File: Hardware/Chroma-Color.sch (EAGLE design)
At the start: 92 parts, among them J1 15-91-1102, J2 87832-6422, J3 1775470-6, J4 D2514-6V0C-AR-WD, J7 26-64-4040, U1 EP4CE6E22C8N, U2 ADP3338AKCZ-3.3-RL, U3 ADP3338AKCZ-2.5-RL, U4 NCV565ST12T3G, U5 M25P40-VMN6TPBCT, X1 ASDMB-50.000MHZ-LC-T

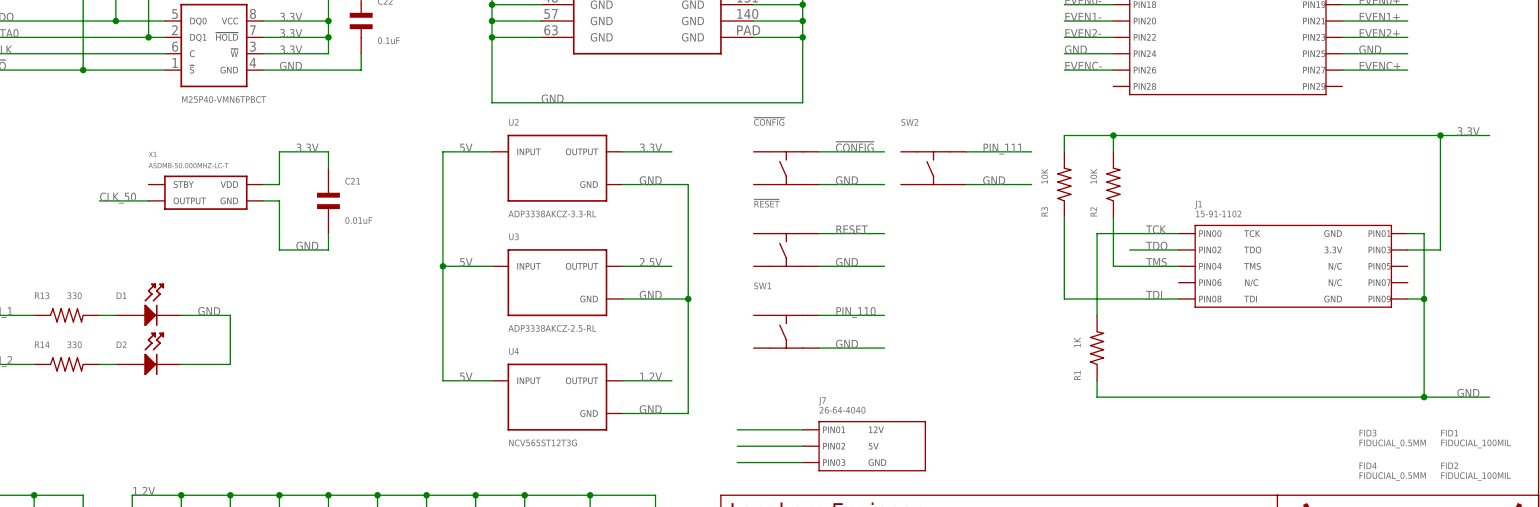
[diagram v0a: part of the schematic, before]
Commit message: Rev2 start. Fixed JTAG programming cable.
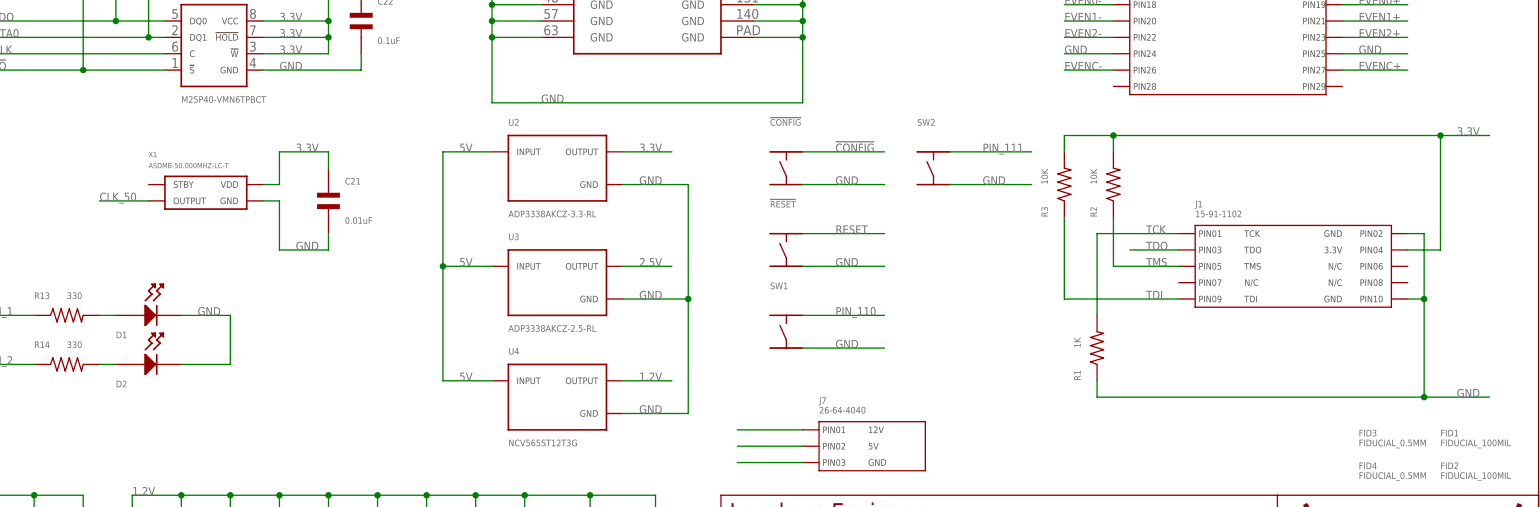
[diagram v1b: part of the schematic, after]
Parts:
- J1: LABEL00 TCK -> (none); LABEL01 GND -> TCK; LABEL02 TDO -> GND; LABEL03 3.3V -> TDO; LABEL04 TMS -> 3.3V; LABEL05 N/C -> TMS; LABEL08 TDI -> N/C; LABEL09 GND -> TDI; LABEL10 (none) -> GND
- U$1: REVNUM REV: 1 -> REV: 2
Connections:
- net 3.3V: now also J1.PIN4; no longer J1.PIN3
- net GND: now also J1.PIN10, J1.PIN2; no longer J1.PIN1, J1.PIN9
- net TCK: now also J1.PIN1; no longer J1.PIN0
- net TDI: now also J1.PIN9; no longer J1.PIN8
- net TDO: now also J1.PIN3; no longer J1.PIN2
- net TMS: now also J1.PIN5; no longer J1.PIN4
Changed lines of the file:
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@@
 <part name="U$1" library="PP_Aesthetics" deviceset="LHE_FRAME" device="">
 <attribute name="DNAME" value="Parker Dillmann"/>
-<attribute name="REVNUM" value="REV: 1"/>
+<attribute name="REVNUM" value="REV: 2"/>
 </part>
 <part name="U$2" library="PP_Aesthetics" deviceset="MF_LOGO" device="LOGO_MEDIUM" value="MF_LOGOLOGO_MEDIUM"/>
@@
 <part name="U1" library="PP_DigitalIC" deviceset="EP4CE6E22C8N" device="" value="EP4CE6E22C8N"/>
 <part name="J1" library="PP_Connectors" deviceset="15-91-1102" device="" value="15-91-1102">
-<attribute name="LABEL00" value="TCK"/>
-<attribute name="LABEL01" value="GND"/>
-<attribute name="LABEL02" value="TDO"/>
-<attribute name="LABEL03" value="3.3V"/>
-<attribute name="LABEL04" value="TMS"/>
-<attribute name="LABEL05" value="N/C"/>
+<attribute name="LABEL01" value="TCK"/>
+<attribute name="LABEL02" value="GND"/>
+<attribute name="LABEL03" value="TDO"/>
+<attribute name="LABEL04" value="3.3V"/>
+<attribute name="LABEL05" value="TMS"/>
 <attribute name="LABEL06" value="N/C"/>
 <attribute name="LABEL07" value="N/C"/>
-<attribute name="LABEL08" value="TDI"/>
-<attribute name="LABEL09" value="GND"/>
+<attribute name="LABEL08" value="N/C"/>
+<attribute name="LABEL09" value="TDI"/>
+<attribute name="LABEL10" value="GND"/>
 </part>
 <part name="R1" library="MF_Passives" deviceset="RESISTOR" device="_0603" value="1K"/>
@@
 </segment>
 <segment>
-<pinref part="J1" gate="G$1" pin="PIN1"/>
-<wire x1="-20.32" y1="66.04" x2="-17.78" y2="66.04" width="0.1524" layer="91"/>
 <wire x1="-17.78" y1="66.04" x2="-17.78" y2="55.88" width="0.1524" layer="91"/>
-<pinref part="J1" gate="G$1" pin="PIN9"/>
 <wire x1="-17.78" y1="55.88" x2="-17.78" y2="40.64" width="0.1524" layer="91"/>
-<wire x1="-20.32" y1="55.88" x2="-17.78" y2="55.88" width="0.1524" layer="91"/>
 <wire x1="-17.78" y1="40.64" x2="-7.62" y2="40.64" width="0.1524" layer="91"/>
 <label x="-12.7" y="40.64" size="1.27" layer="95" font="vector"/>
-<junction x="-17.78" y="55.88"/>
 <pinref part="R1" gate="G$1" pin="P$1"/>
 <wire x1="-17.78" y1="40.64" x2="-68.58" y2="40.64" width="0.1524" layer="91"/>
 <wire x1="-68.58" y1="40.64" x2="-68.58" y2="43.18" width="0.1524" layer="91"/>
 <junction x="-17.78" y="40.64"/>
+<pinref part="J1" gate="G$1" pin="PIN2"/>
+<wire x1="-17.78" y1="66.04" x2="-20.32" y2="66.04" width="0.1524" layer="91"/>
+<pinref part="J1" gate="G$1" pin="PIN10"/>
+<wire x1="-20.32" y1="55.88" x2="-17.78" y2="55.88" width="0.1524" layer="91"/>
+<junction x="-17.78" y="55.88"/>
 </segment>
 <segment>
@@
 <segment>
 <pinref part="!CONFIG" gate="G$1" pin="P$4"/>
-<wire x1="-111.76" y1="73.66" x2="-101.6" y2="73.66" width="0.1524" layer="91"/>
+<wire x1="-114.3" y1="73.66" x2="-101.6" y2="73.66" width="0.1524" layer="91"/>
 <label x="-109.22" y="73.66" size="1.27" layer="95" font="vector"/>
 </segment>
 <segment>
 <pinref part="!RESET" gate="G$1" pin="P$4"/>
-<wire x1="-111.76" y1="60.96" x2="-101.6" y2="60.96" width="0.1524" layer="91"/>
+<wire x1="-114.3" y1="60.96" x2="-101.6" y2="60.96" width="0.1524" layer="91"/>
 <label x="-109.22" y="60.96" size="1.27" layer="95" font="vector"/>
 </segment>
@@
 <segment>
 <pinref part="SW1" gate="G$1" pin="P$4"/>
-<wire x1="-111.76" y1="48.26" x2="-101.6" y2="48.26" width="0.1524" layer="91"/>
+<wire x1="-114.3" y1="48.26" x2="-101.6" y2="48.26" width="0.1524" layer="91"/>
 <label x="-109.22" y="48.26" size="1.27" layer="95" font="vector"/>
 </segment>
 <segment>
 <pinref part="SW2" gate="G$1" pin="P$4"/>
-<wire x1="-88.9" y1="73.66" x2="-78.74" y2="73.66" width="0.1524" layer="91"/>
+<wire x1="-91.44" y1="73.66" x2="-78.74" y2="73.66" width="0.1524" layer="91"/>
 <label x="-86.36" y="73.66" size="1.27" layer="95" font="vector"/>
 </segment>
@@
 </segment>
 <segment>
-<pinref part="J1" gate="G$1" pin="PIN3"/>
-<wire x1="-20.32" y1="63.5" x2="-15.24" y2="63.5" width="0.1524" layer="91"/>
 <wire x1="-15.24" y1="63.5" x2="-15.24" y2="81.28" width="0.1524" layer="91"/>
 <wire x1="-15.24" y1="81.28" x2="-7.62" y2="81.28" width="0.1524" layer="91"/>
@@
 <junction x="-66.04" y="81.28"/>
 <junction x="-15.24" y="81.28"/>
+<pinref part="J1" gate="G$1" pin="PIN4"/>
+<wire x1="-20.32" y1="63.5" x2="-15.24" y2="63.5" width="0.1524" layer="91"/>
 </segment>
 <segment>
@@
 <net name="TCK" class="0">
 <segment>
-<pinref part="J1" gate="G$1" pin="PIN0"/>
+<pinref part="U1" gate="G$11" pin="16"/>
+<wire x1="-208.28" y1="137.16" x2="-198.12" y2="137.16" width="0.1524" layer="91"/>
+<label x="-203.2" y="137.16" size="1.27" layer="95" font="vector"/>
+</segment>
+<segment>
+<pinref part="J1" gate="G$1" pin="PIN1"/>
 <wire x1="-55.88" y1="66.04" x2="-68.58" y2="66.04" width="0.1524" layer="91"/>
 <label x="-60.96" y="66.04" size="1.27" layer="95" font="vector"/>
@@
 <wire x1="-68.58" y1="66.04" x2="-68.58" y2="53.34" width="0.1524" layer="91"/>
 </segment>
-<segment>
-<pinref part="U1" gate="G$11" pin="16"/>
-<wire x1="-208.28" y1="137.16" x2="-198.12" y2="137.16" width="0.1524" layer="91"/>
-<label x="-203.2" y="137.16" size="1.27" layer="95" font="vector"/>
-</segment>
 </net>
 <net name="TDO" class="0">
-<segment>
-<pinref part="J1" gate="G$1" pin="PIN2"/>
-<wire x1="-55.88" y1="63.5" x2="-63.5" y2="63.5" width="0.1524" layer="91"/>
-<label x="-60.96" y="63.5" size="1.27" layer="95" font="vector"/>
-</segment>
 <segment>
 <pinref part="U1" gate="G$11" pin="20"/>
@@
 <label x="-203.2" y="134.62" size="1.27" layer="95" font="vector"/>
 </segment>
+<segment>
+<pinref part="J1" gate="G$1" pin="PIN3"/>
+<wire x1="-55.88" y1="63.5" x2="-63.5" y2="63.5" width="0.1524" layer="91"/>
+<label x="-60.96" y="63.5" size="1.27" layer="95" font="vector"/>
+</segment>
 </net>
 <net name="TMS" class="0">
 <segment>
-<pinref part="J1" gate="G$1" pin="PIN4"/>
-<wire x1="-55.88" y1="60.96" x2="-66.04" y2="60.96" width="0.1524" layer="91"/>
 <label x="-60.96" y="60.96" size="1.27" layer="95" font="vector"/>
 <pinref part="R2" gate="G$1" pin="P$1"/>
 <wire x1="-66.04" y1="68.58" x2="-66.04" y2="60.96" width="0.1524" layer="91"/>
+<pinref part="J1" gate="G$1" pin="PIN5"/>
+<wire x1="-55.88" y1="60.96" x2="-66.04" y2="60.96" width="0.1524" layer="91"/>
 </segment>
 <segment>
@@
 <net name="TDI" class="0">
 <segment>
-<pinref part="J1" gate="G$1" pin="PIN8"/>
 <label x="-60.96" y="55.88" size="1.27" layer="95" font="vector"/>
 <pinref part="R3" gate="G$1" pin="P$1"/>
+<wire x1="-73.66" y1="55.88" x2="-73.66" y2="68.58" width="0.1524" layer="91"/>
+<pinref part="J1" gate="G$1" pin="PIN9"/>
 <wire x1="-55.88" y1="55.88" x2="-73.66" y2="55.88" width="0.1524" layer="91"/>
-<wire x1="-73.66" y1="55.88" x2="-73.66" y2="68.58" width="0.1524" layer="91"/>
 </segment>
 <segment>
@@
 <segment>
 <pinref part="!CONFIG" gate="G$1" pin="P$2"/>
-<wire x1="-111.76" y1="78.74" x2="-101.6" y2="78.74" width="0.1524" layer="91"/>
+<wire x1="-114.3" y1="78.74" x2="-101.6" y2="78.74" width="0.1524" layer="91"/>
 <label x="-109.22" y="78.74" size="1.27" layer="95" font="vector"/>
 </segment>
@@
 <segment>
 <pinref part="!RESET" gate="G$1" pin="P$2"/>
-<wire x1="-111.76" y1="66.04" x2="-101.6" y2="66.04" width="0.1524" layer="91"/>
+<wire x1="-114.3" y1="66.04" x2="-101.6" y2="66.04" width="0.1524" layer="91"/>
 <label x="-109.22" y="66.04" size="1.27" layer="95" font="vector"/>
 </segment>
@@
 <segment>
 <pinref part="SW2" gate="G$1" pin="P$2"/>
-<wire x1="-88.9" y1="78.74" x2="-78.74" y2="78.74" width="0.1524" layer="91"/>
+<wire x1="-91.44" y1="78.74" x2="-78.74" y2="78.74" width="0.1524" layer="91"/>
 <label x="-86.36" y="78.74" size="1.27" layer="95" font="vector"/>
 </segment>
@@
 <segment>
 <pinref part="SW1" gate="G$1" pin="P$2"/>
-<wire x1="-111.76" y1="53.34" x2="-101.6" y2="53.34" width="0.1524" layer="91"/>
+<wire x1="-114.3" y1="53.34" x2="-101.6" y2="53.34" width="0.1524" layer="91"/>
 <label x="-109.22" y="53.34" size="1.27" layer="95" font="vector"/>
 </segment>

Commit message: Fixed 3 PIN Power Connector.
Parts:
- J7: device PP_Connectors:HEADER_01X03MOLEX_KK_4_P1 -> PP_Connectors:CON_01X0326-64-4040(KEYPIN1)
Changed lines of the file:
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@@
 <?xml version="1.0" encoding="utf-8"?>
 <!DOCTYPE eagle SYSTEM "eagle.dtd">
-<eagle version="6.5.0">
+<eagle version="6.6.0">
 <drawing>
 <settings>
@@
 <part name="R7" library="MF_Passives" deviceset="RESISTOR" device="_0603" value="10K"/>
 <part name="J4" library="PP_Connectors" deviceset="SMT_02X07" device="D2514-6V0C-AR-WD" value="D2514-6V0C-AR-WD"/>
-<part name="J7" library="PP_Connectors" deviceset="HEADER_01X03" device="MOLEX_KK_4_P1" value="26-64-4040">
-<attribute name="LABEL01" value="12V"/>
-<attribute name="LABEL02" value="5V"/>
-<attribute name="LABEL03" value="GND"/>
-</part>
 <part name="C10" library="MF_Passives" deviceset="CAPACITOR_NP" device="_0603" value="0.1uF"/>
 <part name="C11" library="MF_Passives" deviceset="CAPACITOR_NP" device="_0603" value="0.1uF"/>
@@
 <part name="FID3" library="MF_Aesthetics" deviceset="FIDUCIAL" device="_0.5MM"/>
 <part name="FID4" library="MF_Aesthetics" deviceset="FIDUCIAL" device="_0.5MM"/>
+<part name="J7" library="PP_Connectors" deviceset="CON_01X03" device="26-64-4040(KEYPIN1)" value="26-64-4040">
+<attribute name="LABEL01" value="12V"/>
+<attribute name="LABEL02" value="5V"/>
+<attribute name="LABEL03" value="GND"/>
+</part>
 </parts>
 <sheets>
@@
 <instance part="R7" gate="G$1" x="-246.38" y="129.54" rot="R270"/>
 <instance part="J4" gate="G$1" x="-45.72" y="147.32"/>
-<instance part="J7" gate="G$1" x="-111.76" y="35.56"/>
 <instance part="C10" gate="G$1" x="-233.68" y="17.78"/>
 <instance part="C11" gate="G$1" x="-396.24" y="17.78"/>
@@
 <instance part="FID3" gate="G$1" x="-27.94" y="35.56"/>
 <instance part="FID4" gate="G$1" x="-27.94" y="30.48"/>
+<instance part="J7" gate="G$1" x="-111.76" y="35.56"/>
 </instances>
 <busses>

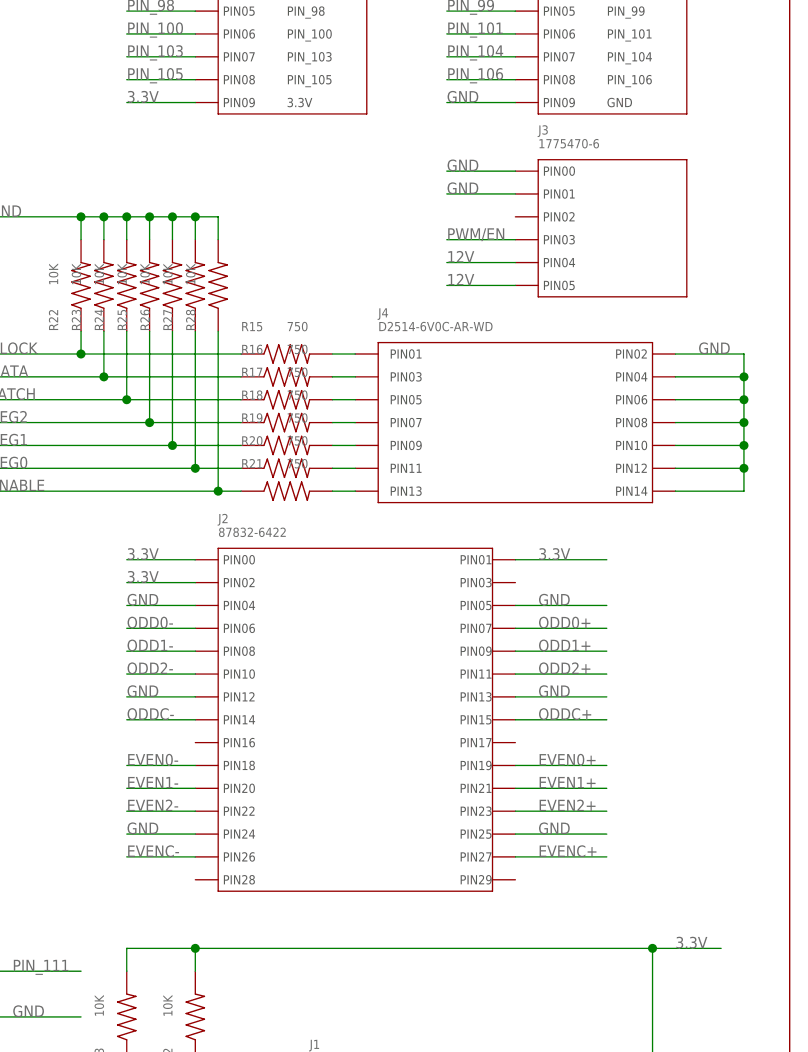
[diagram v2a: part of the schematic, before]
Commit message: Updated connectors to latest library
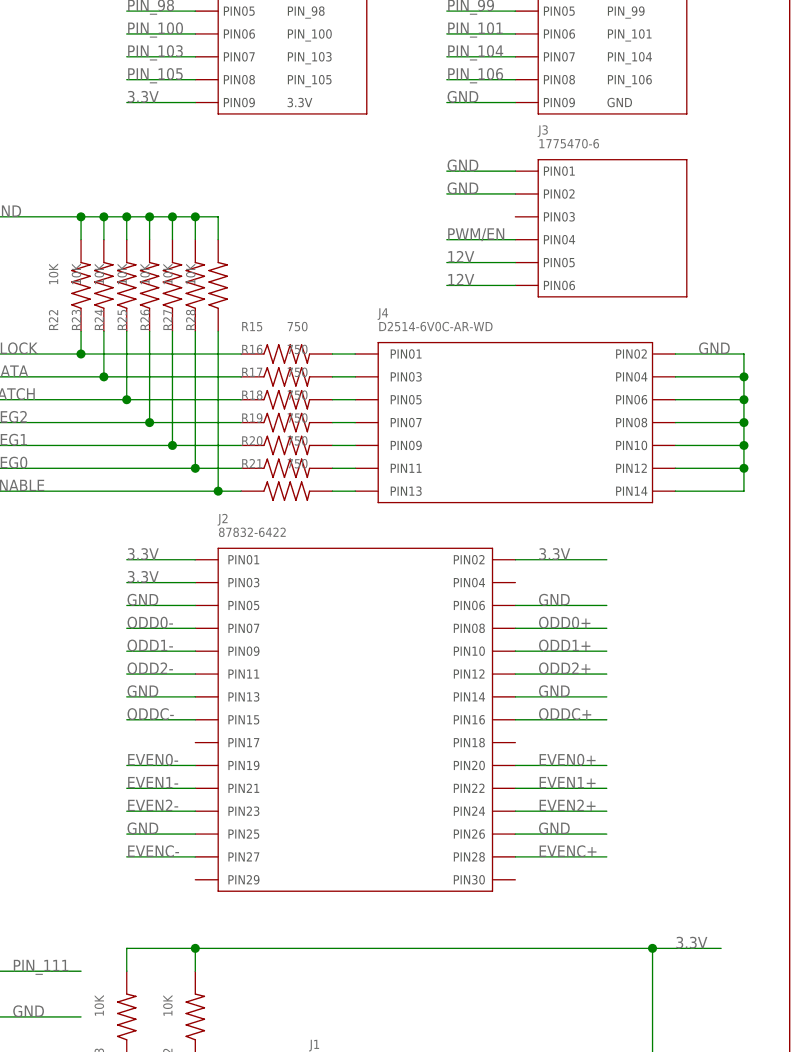
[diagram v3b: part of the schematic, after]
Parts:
- J1: device PP_Connectors:15-91-1102 -> PP_Connectors:CON_02X05_15-91-1102
- J2: device PP_Connectors:87832-6422 -> PP_Connectors:CON_02X15_87832-6422
- J3: device PP_Connectors:1775470-6 -> PP_Connectors:CON_01X06_1775470-6
- J4: device PP_Connectors:SMT_02X07D2514-6V0C-AR-WD -> PP_Connectors:CON_02X07_D2514-6V0C-AR-WD
- J7: device PP_Connectors:CON_01X0326-64-4040(KEYPIN1) -> PP_Connectors:CON_01X03_26-64-4040_(KEYPIN1)
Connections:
- net 12V: now also J3.5, J3.6; no longer J3.PIN4, J3.PIN5
- net GND: now also J3.1, J3.2; no longer J3.PIN0, J3.PIN1
- net PWM/EN: now also J3.4; no longer J3.PIN3
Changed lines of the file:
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@@
 <part name="U$3" library="PP_Aesthetics" deviceset="LHE_LOGO" device="LHE_LOGO"/>
 <part name="U1" library="PP_DigitalIC" deviceset="EP4CE6E22C8N" device="" value="EP4CE6E22C8N"/>
-<part name="J1" library="PP_Connectors" deviceset="15-91-1102" device="" value="15-91-1102">
+<part name="J1" library="PP_Connectors" deviceset="CON_02X05" device="_15-91-1102" value="15-91-1102">
 <attribute name="LABEL01" value="TCK"/>
 <attribute name="LABEL02" value="GND"/>
@@
 <part name="X1" library="PP_FreqCtrl" deviceset="ASDMB" device="" value="ASDMB-50.000MHZ-LC-T"/>
 <part name="C21" library="MF_Passives" deviceset="CAPACITOR_NP" device="_0603" value="0.01uF"/>
-<part name="J2" library="PP_Connectors" deviceset="87832-6422" device="" value="87832-6422"/>
-<part name="J3" library="PP_Connectors" deviceset="1775470-6" device="" value="1775470-6"/>
+<part name="J2" library="PP_Connectors" deviceset="CON_02X15" device="_87832-6422" value="87832-6422"/>
 <part name="C22" library="MF_Passives" deviceset="CAPACITOR_NP" device="_0603" value="0.1uF"/>
 <part name="C23" library="MF_Passives" deviceset="CAPACITOR_NP" device="_0603" value="0.1uF"/>
@@
 <part name="!RESET" library="MF_Switches" deviceset="TACT" device="_4.2MM"/>
 <part name="R7" library="MF_Passives" deviceset="RESISTOR" device="_0603" value="10K"/>
-<part name="J4" library="PP_Connectors" deviceset="SMT_02X07" device="D2514-6V0C-AR-WD" value="D2514-6V0C-AR-WD"/>
+<part name="J4" library="PP_Connectors" deviceset="CON_02X07" device="_D2514-6V0C-AR-WD" value="D2514-6V0C-AR-WD"/>
 <part name="C10" library="MF_Passives" deviceset="CAPACITOR_NP" device="_0603" value="0.1uF"/>
 <part name="C11" library="MF_Passives" deviceset="CAPACITOR_NP" device="_0603" value="0.1uF"/>
@@
 <part name="FID3" library="MF_Aesthetics" deviceset="FIDUCIAL" device="_0.5MM"/>
 <part name="FID4" library="MF_Aesthetics" deviceset="FIDUCIAL" device="_0.5MM"/>
-<part name="J7" library="PP_Connectors" deviceset="CON_01X03" device="26-64-4040(KEYPIN1)" value="26-64-4040">
+<part name="J7" library="PP_Connectors" deviceset="CON_01X03" device="_26-64-4040_(KEYPIN1)" value="26-64-4040">
 <attribute name="LABEL01" value="12V"/>
 <attribute name="LABEL02" value="5V"/>
 <attribute name="LABEL03" value="GND"/>
 </part>
+<part name="J3" library="PP_Connectors" deviceset="CON_01X06" device="_1775470-6" value="1775470-6"/>
 </parts>
 <sheets>
@@
 <instance part="C21" gate="G$1" x="-187.96" y="71.12"/>
 <instance part="J2" gate="G$1" x="-63.5" y="124.46"/>
-<instance part="J3" gate="G$1" x="-27.94" y="167.64"/>
 <instance part="C22" gate="G$1" x="-182.88" y="99.06"/>
 <instance part="C23" gate="G$1" x="-241.3" y="17.78"/>
@@
 <instance part="FID4" gate="G$1" x="-27.94" y="30.48"/>
 <instance part="J7" gate="G$1" x="-111.76" y="35.56"/>
+<instance part="J3" gate="G$1" x="-27.94" y="167.64"/>
 </instances>
 <busses>
@@
 </segment>
 <segment>
-<pinref part="J3" gate="G$1" pin="PIN1"/>
 <wire x1="-38.1" y1="165.1" x2="-30.48" y2="165.1" width="0.1524" layer="91"/>
 <label x="-38.1" y="165.1" size="1.27" layer="95" font="vector"/>
-</segment>
-<segment>
-<pinref part="J3" gate="G$1" pin="PIN0"/>
+<pinref part="J3" gate="G$1" pin="2"/>
+</segment>
+<segment>
 <wire x1="-30.48" y1="167.64" x2="-38.1" y2="167.64" width="0.1524" layer="91"/>
 <label x="-38.1" y="167.64" size="1.27" layer="95" font="vector"/>
+<pinref part="J3" gate="G$1" pin="1"/>
 </segment>
 <segment>
@@
 <net name="PWM/EN" class="0">
 <segment>
-<pinref part="J3" gate="G$1" pin="PIN3"/>
 <wire x1="-38.1" y1="160.02" x2="-30.48" y2="160.02" width="0.1524" layer="91"/>
 <label x="-38.1" y="160.02" size="1.27" layer="95" font="vector"/>
+<pinref part="J3" gate="G$1" pin="4"/>
 </segment>
 <segment>
@@
 <net name="12V" class="0">
 <segment>
-<pinref part="J3" gate="G$1" pin="PIN4"/>
 <wire x1="-30.48" y1="157.48" x2="-38.1" y2="157.48" width="0.1524" layer="91"/>
 <label x="-38.1" y="157.48" size="1.27" layer="95" font="vector"/>
-</segment>
-<segment>
-<pinref part="J3" gate="G$1" pin="PIN5"/>
+<pinref part="J3" gate="G$1" pin="5"/>
+</segment>
+<segment>
 <wire x1="-38.1" y1="154.94" x2="-30.48" y2="154.94" width="0.1524" layer="91"/>
 <label x="-38.1" y="154.94" size="1.27" layer="95" font="vector"/>
-</segment>
-<segment>
+<pinref part="J3" gate="G$1" pin="6"/>
+</segment>
+<segment>
